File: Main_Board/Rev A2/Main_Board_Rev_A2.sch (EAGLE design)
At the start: 207 parts, among them J1 90814-0208, J12 22-27-2061-06, J15 1241050-5, J2 90814-0206, J3 90814-0208, J4 5504F1-09S-02A-03, J5 22-05-7048-04, J6 22-05-7048-04, J7 22-05-7058-05, J8 22-05-7048-04, K1 G6K-2G-Y, K2 G6K-2G-Y, K3 G6K-2G-Y, K4 G6K-2G-Y, P1 RB1-125BAG1A, SW1 B3FS-1015, SW2 B3FS-1015, T1 MMBT2222AL, U1 LT3686HDDPBF, U10 SN74LVC2G17DBVR, U11 MCP2561-E/SN, U12 TLV313, U2 TPL0401A, U3 SN74LVC3G17DCTR, U4 SN74LVC3G17DCTR, U5 LT3686HDDPBF, U6 LPC1768FBD100, U7 AT24C512C-SSHM-B, U8 SN74LVC3G17DCTR, U9 SN74LVC2G17DBVR, X1 ASE_50, X12 22-05-7028-02, X13 22-05-7028-02, X14 22-05-7038-03, X15 22-05-7038-03, X2 FC-135, X3 ASE-12, X4 MSTBA2, X5 22-05-7028-02, X6 USB3075-30-A, X7 3000, X8 22-05-7028-02

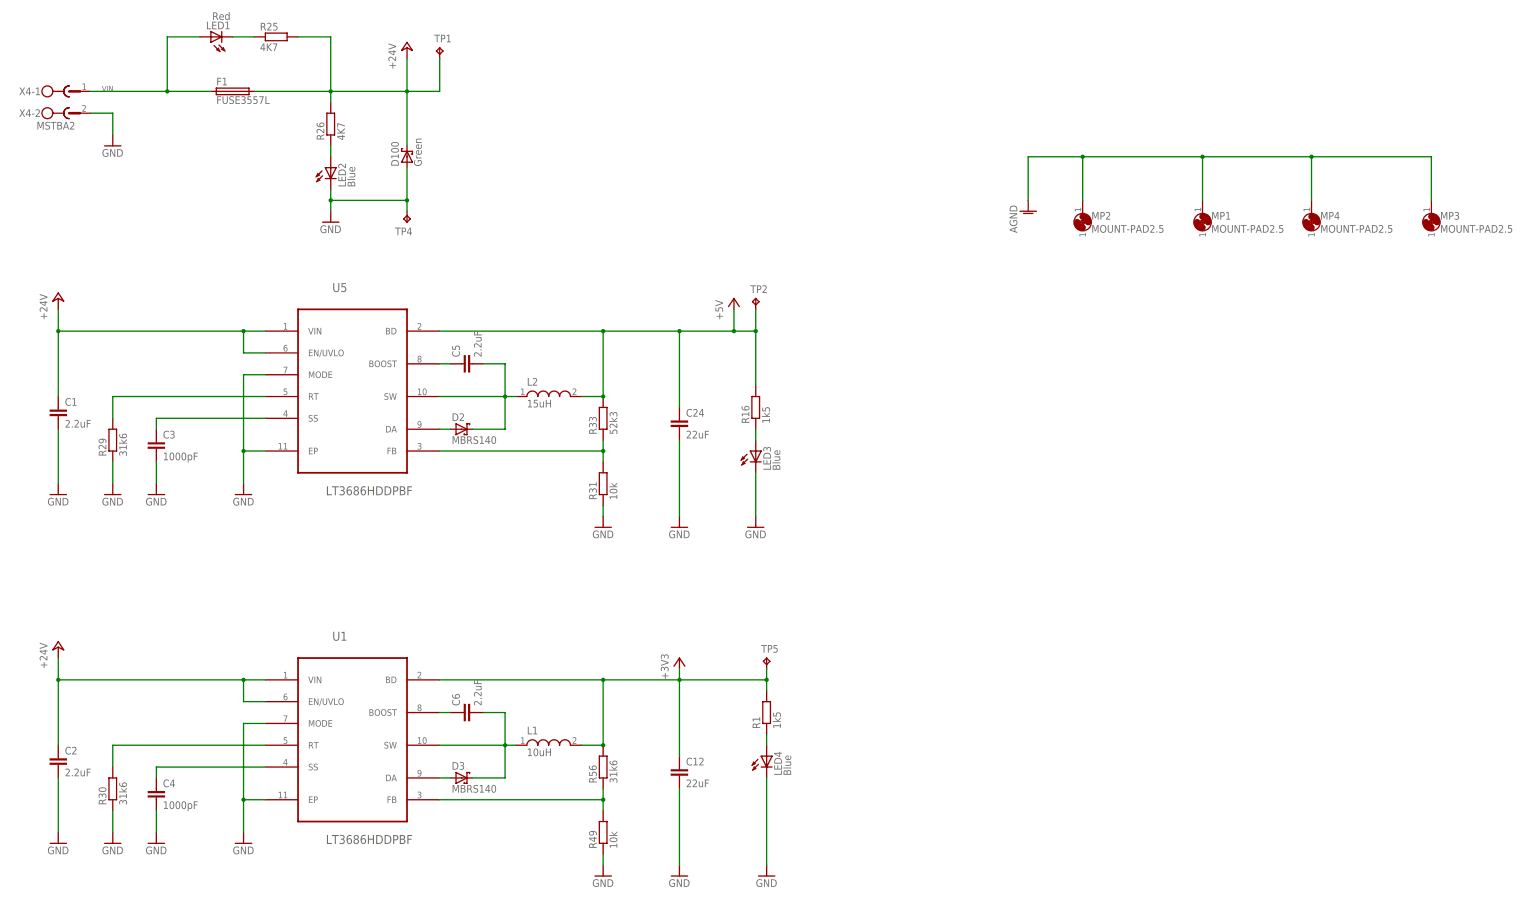
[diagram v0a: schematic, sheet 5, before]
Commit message: Add description on the connector
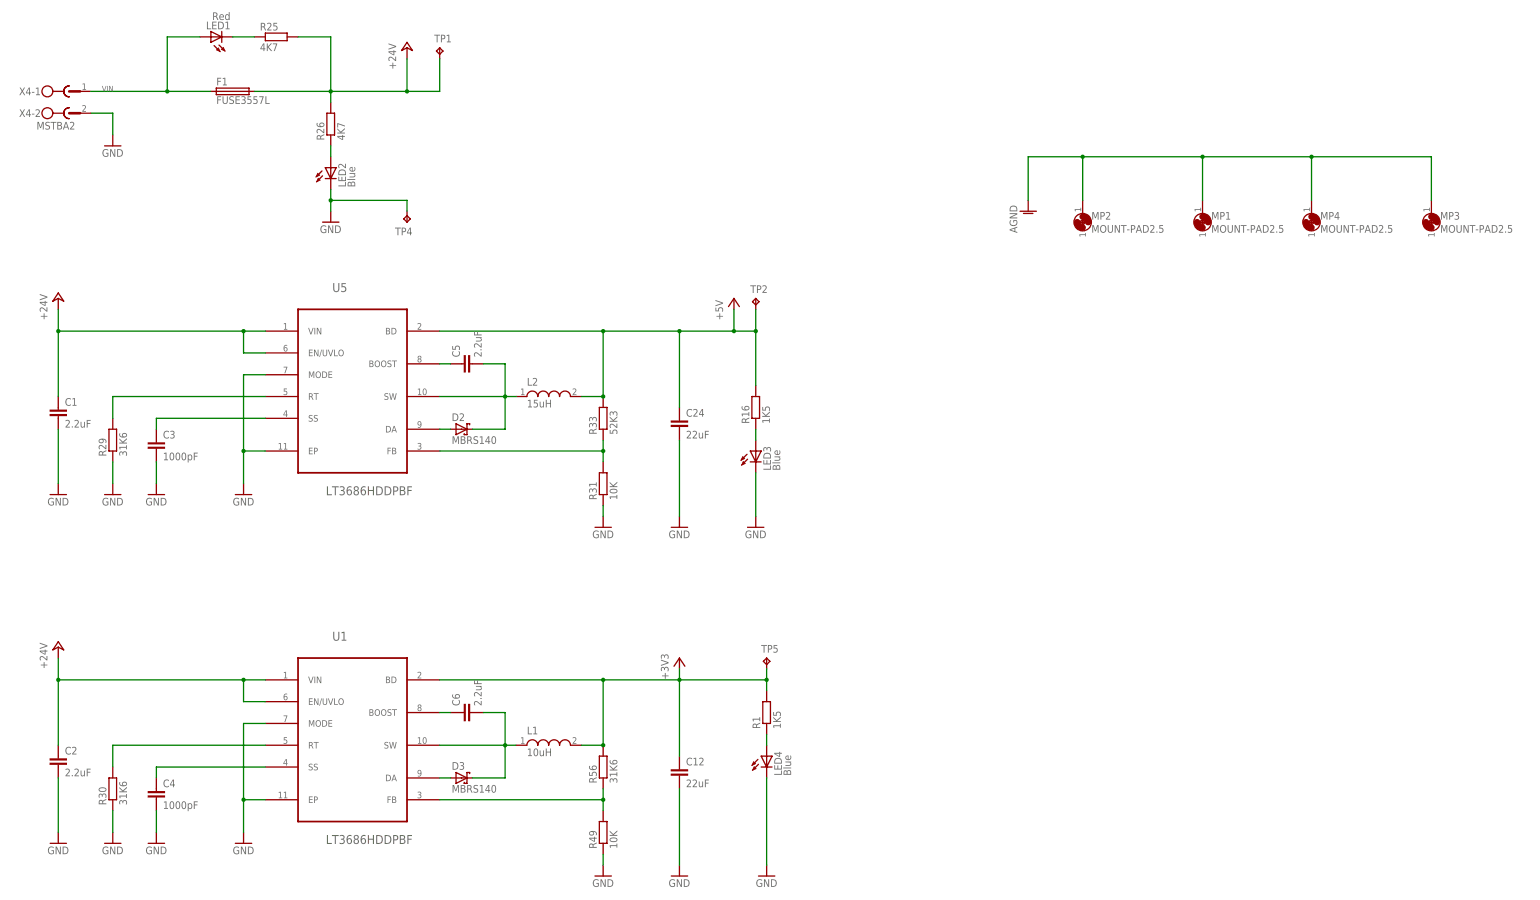
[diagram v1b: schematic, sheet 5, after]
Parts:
- removed D100: Green, diode:STPS3L40UF
- C10, C11: MPN (none) -> MC0603X475K100CT; OC_NEWARK (none) -> 06X6198
- C101, C102, C103, C104, C105, C106, C107, C108, C109, C129, C130, C131, C132, C133, C134: MPN (none) -> MC0603B104K160CT; OC_NEWARK (none) -> 06R4923
- C12, C24: MPN MCMT21N220F250CT -> (none); OC_NEWARK 23T7233 -> unknown
- C37, C38: MPN MC0603B104K250CT -> MC0603B104K160CT; OC_NEWARK 06R4925 -> 06R4923
- F1: MPN (none) -> 3557; OC_NEWARK (none) -> 22M2711
- JP1, JP2, JP4, JP5, MP1, MP2, MP3, MP4, TP1, TP4, U$2: OC_NEWARK (none) -> unknown
- K1, K2, K3, K4: MF (none) -> OMRON COMPONENTS USA; MPN (none) -> G6K-2G-YDC24 BY OMR; OC_NEWARK (none) -> 17C6944
- LED1: MPN (none) -> OVS-0608; OC_NEWARK (none) -> 15R2208
- LED2, LED6, LED7, LED8, LED9: MPN (none) -> OVS-0603; OC_NEWARK (none) -> 15R2205
- LED3, LED4: device led:LEDCHIP-LED0603 -> led:LEDCHIPLED_0603; MPN OVS-0604 -> OVS-0603; OC_FARNELL 1716771 -> (none); OC_NEWARK 15R2206 -> 15R2205
- LED5: value (none) -> Blue; MPN (none) -> OVS-0603; OC_NEWARK (none) -> 15R2205
- R1, R16: value 1k5 -> 1K5; MF Multicomp Passives -> (none); MPN MC0063W060311K5 -> MCMR06X1501FTL; OC_NEWARK 58K4488 -> 86T3542
- R10, R11, R12, R13, R8, R9: MPN (none) -> MCMR06X1001FTL; OC_NEWARK (none) -> 86T3505
- R108, R109, R110, R111, R15, R4, R41, R43, R45, R47, R5, R6, R7: MPN (none) -> MCMR06X1000FTL; OC_NEWARK (none) -> 86T3504
- R14, R2, R25, R26, R42, R44: MPN (none) -> MCMR06X4701FTL; OC_NEWARK (none) -> 86T3649
- R29, R30, R56: value 31k6 -> 31K6; MF Multicomp Passives -> (none); MPN MC0063W060311K5 -> MC0603SAF3162T5E; OC_NEWARK 58K4488 -> 79M5962
- R3, R35, R36: MPN (none) -> MCMR06X33R0FTL; OC_NEWARK (none) -> 86T3614
- R31, R49: value 10k -> 10K
- R32, R34, R37, R40: MPN (none) -> MCMR06X1002FTL; OC_NEWARK (none) -> 86T3506
- R33: value 52k3 -> 52K3
- R38, R39, R50, R51, R52, R53: MPN (none) -> MCMR06X1501FTL; OC_NEWARK (none) -> 86T3542
- R46, R48: value 4k7 -> 4K7; MPN (none) -> MCMR06X4701FTL; OC_NEWARK (none) -> 86T3649
- R72, R74, R75: MPN MCMR06X1000FTL -> MCMR06X1001FTL; OC_NEWARK 86T3504 -> 86T3505
- SW1, SW2: value B3FS-1015 -> B3FS-1050; device Switch_SMT:B3FS-1015 -> Switch_SMT:B3FS-1050; MF (none) -> FARNELL; MPN (none) -> B3FS-1050; OC_NEWARK unknown -> 18J2451
- T1: MPN (none) -> MMBT2222ALT3G; OC_NEWARK (none) -> 10N9478
- U10, U3, U4, U9: MF (none) -> TEXAS INSTRUMENTS
- U2: MPN (none) -> ISL90727WIE627Z-T7A; OC_NEWARK (none) -> 82Y6761
- X12, X13, X5, X8: MPN (none) -> 22-05-7028; OC_NEWARK (none) -> 25M1728
- X14, X15: MPN (none) -> 22-05-7038; OC_NEWARK (none) -> 26M6362
- X6: MPN (none) -> USB3075-30-A; OC_NEWARK (none) -> 58T0863
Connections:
- net +24V: no longer D100.C
- net GND: no longer D100.A

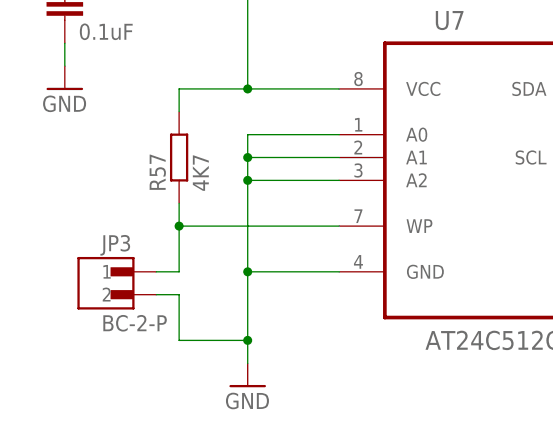
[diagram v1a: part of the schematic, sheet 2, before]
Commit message: Name sheet 6 and add +5V output for ethernet switch
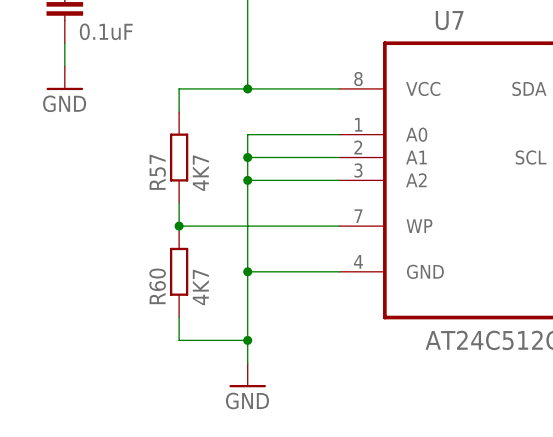
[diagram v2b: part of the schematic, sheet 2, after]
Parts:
- removed JP3: BC-2-P, exmachina:BC-2-P
- added J9: 22-05-7028-02, con-molex:22-05-7028-02
- added R60: 4K7, rcl:R-EU_R0603
- R77, R78: value 1K8 -> 150
- R79, R80: value 1K2 -> 100K
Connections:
- net +5V: now also J9-1.S
- net GND: now also J9-2.S, R60.1; no longer JP3.2
- net N$47: now also R60.2; no longer JP3.1
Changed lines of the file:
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@@
 </part>
 <part name="GND86" library="supply1" deviceset="GND" device=""/>
-<part name="JP3" library="exmachina" deviceset="BC-2?" device="-P">
-<attribute name="MF" value=""/>
-<attribute name="MPN" value=""/>
-<attribute name="OC_NEWARK" value="unknown"/>
-</part>
 <part name="R68" library="rcl" deviceset="R-EU_" device="R0603" value="0R">
 <attribute name="MF" value=""/>
@@
 <attribute name="OC_NEWARK" value="95Y0395"/>
 </part>
-<part name="R77" library="rcl" deviceset="R-EU_" device="R0603" value="1K8">
+<part name="R77" library="rcl" deviceset="R-EU_" device="R0603" value="150">
 <attribute name="MF" value=""/>
 <attribute name="MPN" value="MCMR06X1801FTL"/>
 <attribute name="OC_NEWARK" value="86T3556"/>
 </part>
-<part name="R78" library="rcl" deviceset="R-EU_" device="R0603" value="1K8">
+<part name="R78" library="rcl" deviceset="R-EU_" device="R0603" value="150">
 <attribute name="MF" value=""/>
 <attribute name="MPN" value="MCMR06X1801FTL"/>
 <attribute name="OC_NEWARK" value="86T3556"/>
 </part>
-<part name="R79" library="rcl" deviceset="R-EU_" device="R0603" value="1K2">
+<part name="R79" library="rcl" deviceset="R-EU_" device="R0603" value="100K">
 <attribute name="MF" value=""/>
 <attribute name="MPN" value="MCMR06X1201FTL"/>
 <attribute name="OC_NEWARK" value="86T3525"/>
 </part>
-<part name="R80" library="rcl" deviceset="R-EU_" device="R0603" value="1K2">
+<part name="R80" library="rcl" deviceset="R-EU_" device="R0603" value="100K">
 <attribute name="MF" value=""/>
 <attribute name="MPN" value="MCMR06X1201FTL"/>
@@
 <attribute name="OC_NEWARK" value="15R2205"/>
 </part>
+<part name="R60" library="rcl" deviceset="R-EU_" device="R0603" value="4K7">
+<attribute name="MF" value=""/>
+<attribute name="MPN" value="MCMR06X4701FTL"/>
+<attribute name="OC_NEWARK" value="86T3649"/>
+</part>
+<part name="J9" library="con-molex" deviceset="22-?-02" device="05-7028"/>
+<part name="GND87" library="supply1" deviceset="GND" device=""/>
+<part name="+3V15" library="supply1" deviceset="+5V" device=""/>
 </parts>
 <sheets>
@@
 <instance part="AGND2" gate="VR1" x="109.22" y="45.72"/>
 <instance part="AGND4" gate="VR1" x="45.72" y="154.94"/>
+<instance part="J9" gate="-1" x="27.94" y="137.16" rot="MR0"/>
+<instance part="J9" gate="-2" x="27.94" y="132.08" rot="MR0"/>
+<instance part="GND87" gate="1" x="35.56" y="127"/>
+<instance part="+3V15" gate="1" x="35.56" y="147.32"/>
 </instances>
 <busses>
@@
 <wire x1="88.9" y1="68.58" x2="88.9" y2="81.28" width="0.1524" layer="91"/>
 </segment>
+<segment>
+<pinref part="J9" gate="-2" pin="S"/>
+<pinref part="GND87" gate="1" pin="GND"/>
+<wire x1="30.48" y1="132.08" x2="35.56" y2="132.08" width="0.1524" layer="91"/>
+<wire x1="35.56" y1="132.08" x2="35.56" y2="129.54" width="0.1524" layer="91"/>
+</segment>
 </net>
 <net name="+3V3" class="2">
@@
 <pinref part="C13" gate="G$1" pin="1"/>
 </segment>
+<segment>
+<pinref part="J9" gate="-1" pin="S"/>
+<pinref part="+3V15" gate="1" pin="+5V"/>
+<wire x1="30.48" y1="137.16" x2="35.56" y2="137.16" width="0.1524" layer="91"/>
+<wire x1="35.56" y1="137.16" x2="35.56" y2="144.78" width="0.1524" layer="91"/>
+</segment>
 </net>
 <net name="CAN_X_N" class="1">
@@
 </instance>
 <instance part="GND86" gate="1" x="60.96" y="91.44"/>
-<instance part="JP3" gate="G$1" x="17.78" y="17.78">
-<attribute name="OC_NEWARK" x="17.78" y="17.78" size="1.778" layer="96" display="off"/>
-<attribute name="MF" x="17.78" y="17.78" size="1.778" layer="96" display="off"/>
-<attribute name="MPN" x="17.78" y="17.78" size="1.778" layer="96" display="off"/>
-</instance>
 <instance part="R68" gate="G$1" x="281.94" y="68.58" rot="R180">
 <attribute name="OC_NEWARK" x="281.94" y="68.58" size="1.778" layer="96" display="off"/>
@@
 </instance>
 <instance part="+3V14" gate="G$1" x="358.14" y="66.04"/>
+<instance part="R60" gate="G$1" x="25.4" y="17.78" rot="R90">
+<attribute name="OC_NEWARK" x="25.4" y="17.78" size="1.778" layer="96" display="off"/>
+<attribute name="MF" x="25.4" y="17.78" size="1.778" layer="96" display="off"/>
+<attribute name="MPN" x="25.4" y="17.78" size="1.778" layer="96" display="off"/>
+</instance>
 </instances>
 <busses>
@@
 <junction x="33.02" y="27.94"/>
 <junction x="33.02" y="10.16"/>
-<pinref part="JP3" gate="G$1" pin="2"/>
-<wire x1="22.86" y1="15.24" x2="25.4" y2="15.24" width="0.1524" layer="91"/>
-<wire x1="25.4" y1="15.24" x2="25.4" y2="10.16" width="0.1524" layer="91"/>
 <wire x1="25.4" y1="10.16" x2="33.02" y2="10.16" width="0.1524" layer="91"/>
+<pinref part="R60" gate="G$1" pin="1"/>
+<wire x1="25.4" y1="12.7" x2="25.4" y2="10.16" width="0.1524" layer="91"/>
 </segment>
 <segment>
@@
 <wire x1="25.4" y1="25.4" x2="25.4" y2="22.86" width="0.1524" layer="91"/>
 <wire x1="25.4" y1="22.86" x2="43.18" y2="22.86" width="0.1524" layer="91"/>
+<pinref part="R60" gate="G$1" pin="2"/>
 <junction x="25.4" y="22.86"/>
-<pinref part="JP3" gate="G$1" pin="1"/>
-<wire x1="22.86" y1="17.78" x2="25.4" y2="17.78" width="0.1524" layer="91"/>
-<wire x1="25.4" y1="17.78" x2="25.4" y2="22.86" width="0.1524" layer="91"/>
 </segment>
 </net>
@@
 </sheet>
 <sheet>
+<description>Programation interface</description>
 <plain>
 <text x="86.36" y="246.38" size="1.778" layer="97">USB</text>

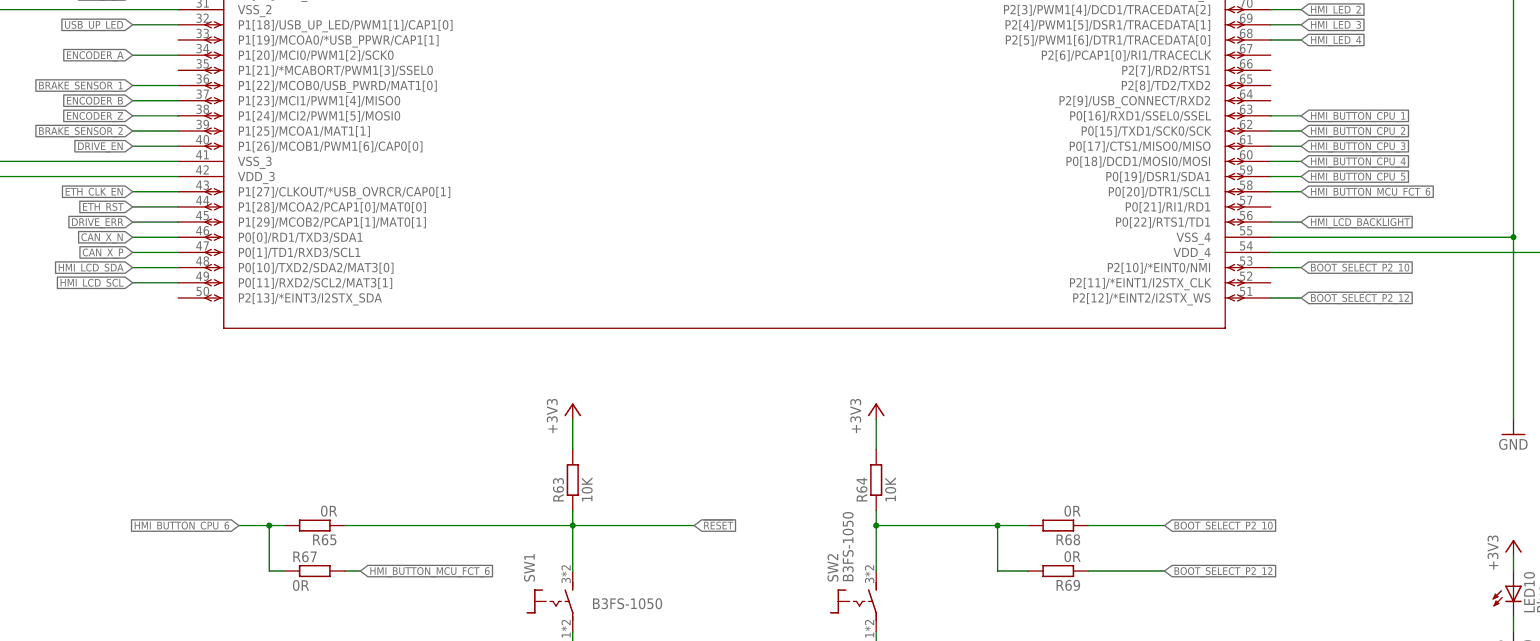
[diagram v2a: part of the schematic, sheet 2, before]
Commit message: Renamed HMI_BUTTON_CPU nets to HMI_BUTTON_ISO
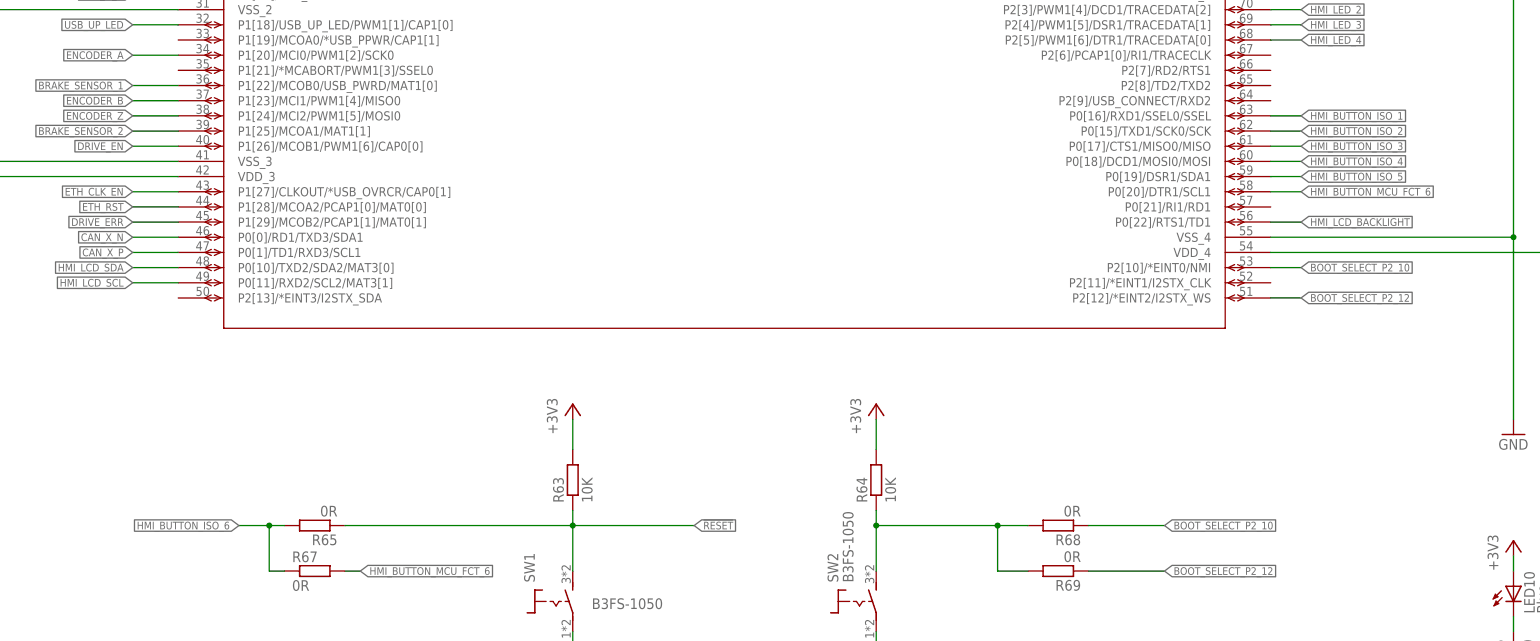
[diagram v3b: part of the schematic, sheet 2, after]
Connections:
- net HMI_BUTTON_CPU_1 renamed HMI_BUTTON_ISO_1
- net HMI_BUTTON_CPU_2 renamed HMI_BUTTON_ISO_2
- net HMI_BUTTON_CPU_3 renamed HMI_BUTTON_ISO_3
- net HMI_BUTTON_CPU_4 renamed HMI_BUTTON_ISO_4
- net HMI_BUTTON_CPU_5 renamed HMI_BUTTON_ISO_5
- net HMI_BUTTON_CPU_6 renamed HMI_BUTTON_ISO_6
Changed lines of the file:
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@@
 </segment>
 </net>
-<net name="HMI_BUTTON_CPU_1" class="0">
+<net name="HMI_BUTTON_ISO_1" class="0">
 <segment>
 <pinref part="U6" gate="A" pin="P0[16]/RXD1/SSEL0/SSEL"/>
@@
 </segment>
 </net>
-<net name="HMI_BUTTON_CPU_2" class="0">
+<net name="HMI_BUTTON_ISO_2" class="0">
 <segment>
 <pinref part="U6" gate="A" pin="P0[15]/TXD1/SCK0/SCK"/>
@@
 </segment>
 </net>
-<net name="HMI_BUTTON_CPU_3" class="0">
+<net name="HMI_BUTTON_ISO_3" class="0">
 <segment>
 <pinref part="U6" gate="A" pin="P0[17]/CTS1/MISO0/MISO"/>
@@
 </segment>
 </net>
-<net name="HMI_BUTTON_CPU_4" class="0">
+<net name="HMI_BUTTON_ISO_4" class="0">
 <segment>
 <pinref part="U6" gate="A" pin="P0[18]/DCD1/MOSI0/MOSI"/>
@@
 </segment>
 </net>
-<net name="HMI_BUTTON_CPU_5" class="0">
+<net name="HMI_BUTTON_ISO_5" class="0">
 <segment>
 <pinref part="U6" gate="A" pin="P0[19]/DSR1/SDA1"/>
@@
 </segment>
 </net>
-<net name="HMI_BUTTON_CPU_6" class="0">
+<net name="HMI_BUTTON_ISO_6" class="0">
 <segment>
 <pinref part="R65" gate="G$1" pin="2"/>
@@
 </segment>
 </net>
-<net name="HMI_BUTTON_CPU_4" class="0">
+<net name="HMI_BUTTON_ISO_4" class="0">
 <segment>
 <pinref part="U3" gate="A" pin="1A"/>
@@
 </segment>
 </net>
-<net name="HMI_BUTTON_CPU_5" class="0">
+<net name="HMI_BUTTON_ISO_5" class="0">
 <segment>
 <pinref part="U3" gate="A" pin="2A"/>
@@
 </segment>
 </net>
-<net name="HMI_BUTTON_CPU_6" class="0">
+<net name="HMI_BUTTON_ISO_6" class="0">
 <segment>
 <pinref part="U3" gate="A" pin="3A"/>
@@
 </segment>
 </net>
-<net name="HMI_BUTTON_CPU_1" class="0">
+<net name="HMI_BUTTON_ISO_1" class="0">
 <segment>
 <pinref part="U4" gate="A" pin="1A"/>
@@
 </segment>
 </net>
-<net name="HMI_BUTTON_CPU_2" class="0">
+<net name="HMI_BUTTON_ISO_2" class="0">
 <segment>
 <pinref part="U4" gate="A" pin="2A"/>
@@
 </segment>
 </net>
-<net name="HMI_BUTTON_CPU_3" class="0">
+<net name="HMI_BUTTON_ISO_3" class="0">
 <segment>
 <pinref part="U4" gate="A" pin="3A"/>
